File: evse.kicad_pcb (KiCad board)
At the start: 2 copper layers, 100 x 100 mm, 121 parts, among them IC1 LF353, IC2 ATmega328P, IC3 LM358, IC8 HCPL-2731S, J1 ISP, J2 Conn_01x04_Pin, J3 KF128-2.54-2P, J4 T44009, J5 T44009, J6 T44009, J7 T44009, J8 T44009, J9 T44009, K1 HF186F/12-HCTF, K2 HF186F/12-HCTF, M1 MOV, M2 MOV, M3 MOV, Q2 MMBT2222A, Q3 MMBT2222A, U1 AP63205WU, U2 TC1044S, U3 MCP9808, Y1 16MHz

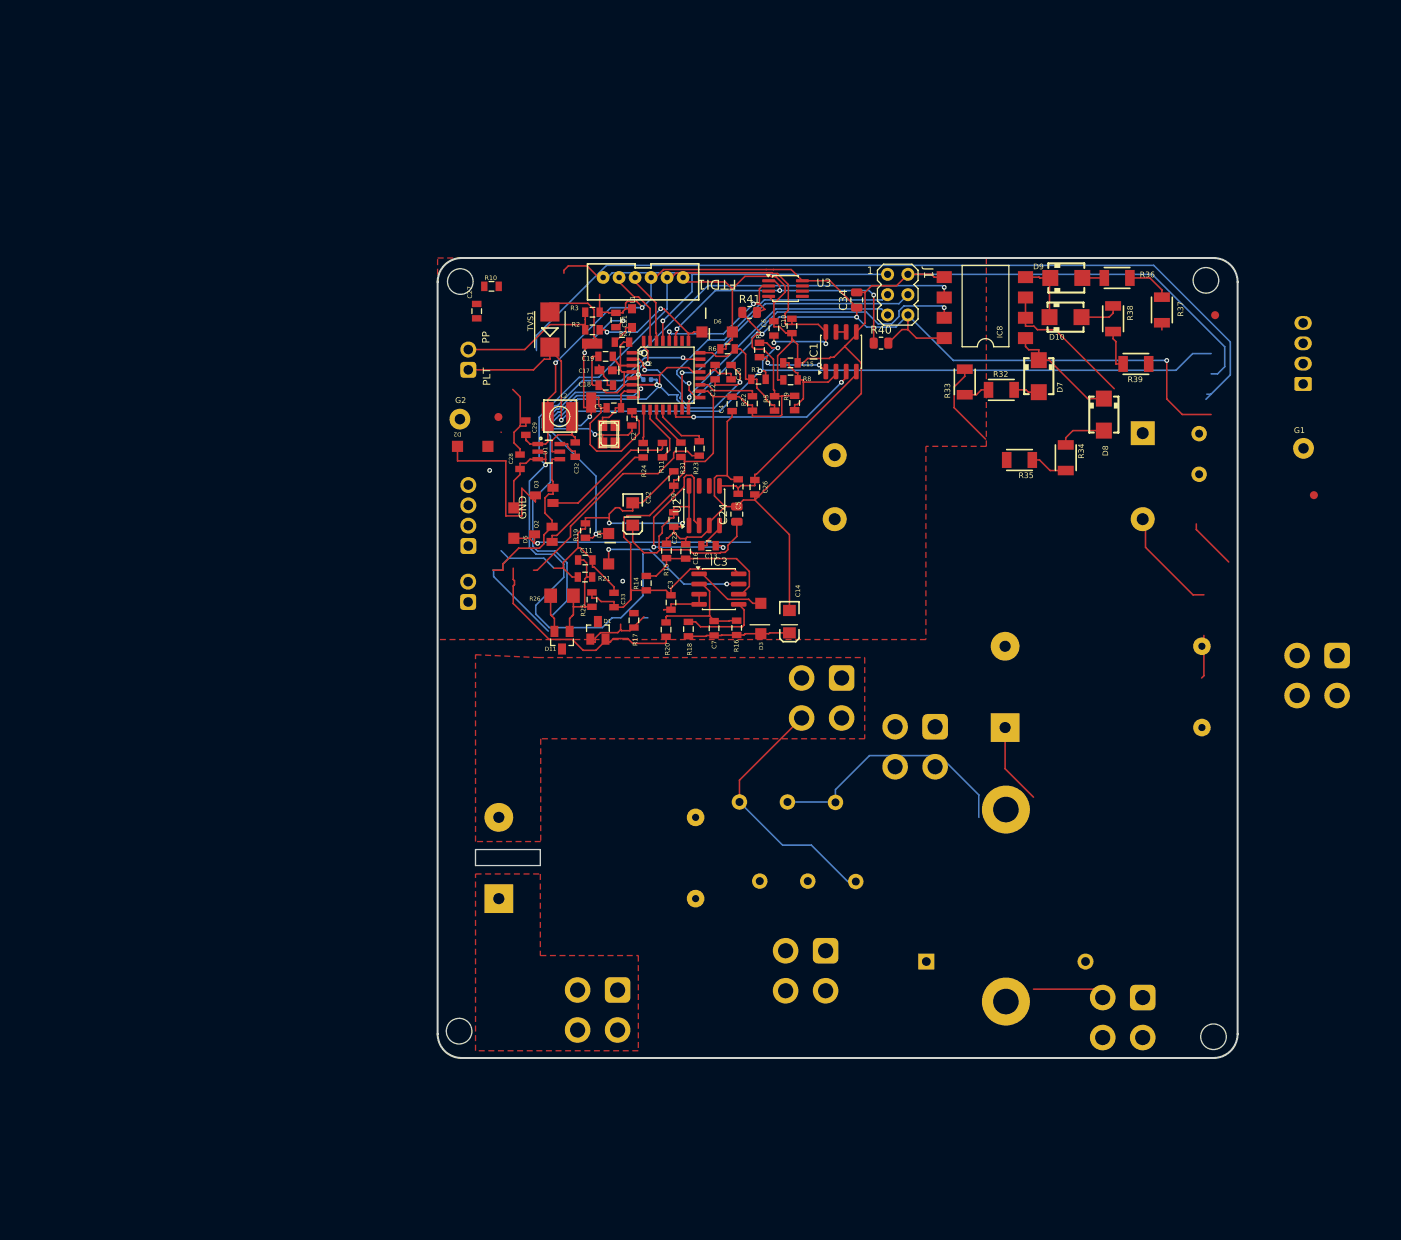
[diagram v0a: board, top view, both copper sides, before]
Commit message: Add DL-CT08CL19 GFCI transformer
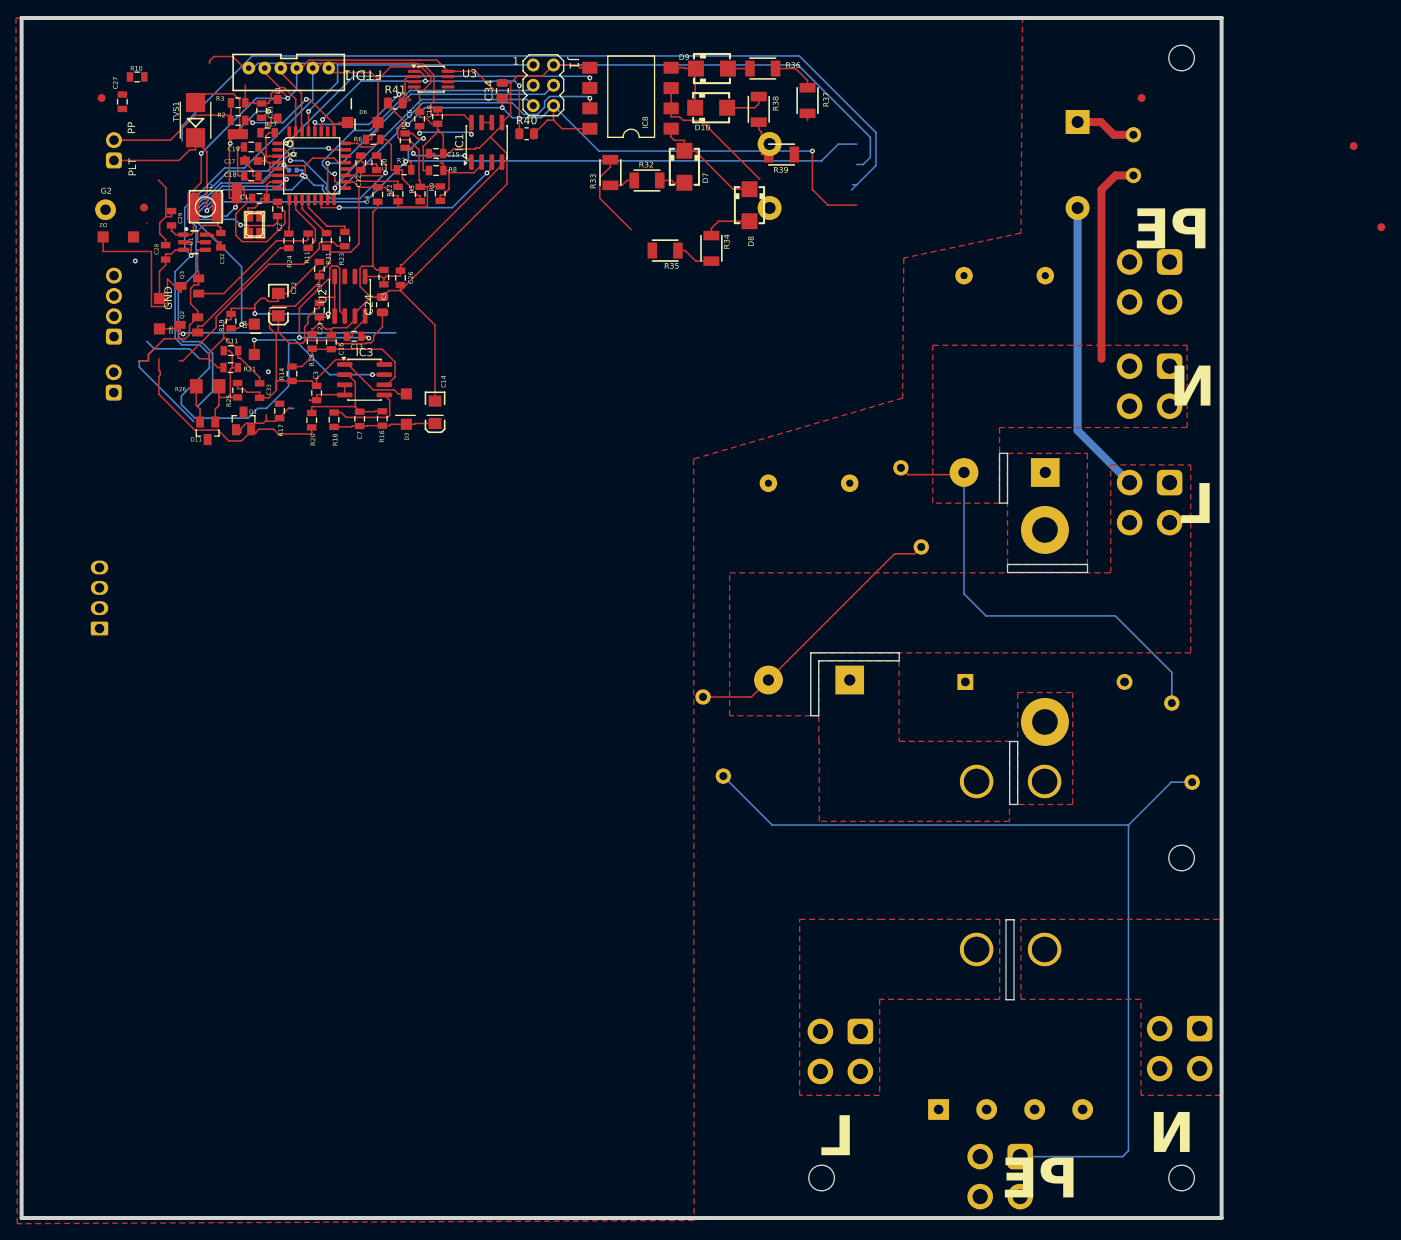
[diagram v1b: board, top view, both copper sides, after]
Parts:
- removed G1: M01PTH, 1X01
- added FID4: FIDUCIAL1X2.5, FIDUCIAL-1X2.5, F.Cu at (160.0, 30.0)
- added FID4: FIDUCIAL1X2.5, FIDUCIAL-1X2.5, F.Cu at (30.0, 30.0)
- added GFCI_CT2: DL-CT08CL19-1000/1, DL_CT:DL-CT08CL19-1000-1, B.Cu at (143.6, 136.4)
- PS1: footprint OpenEVSE:Converter_ACDC_MeanWell_IRM-10-12_THT -> Converter_ACDC:Converter_ACDC_MeanWell_IRM-10-xx_THT
- moved J2 153.5 mm to (29.7, 96.3)
- moved ? 151.5 mm to (165.0, 25.0)
- moved UNK_HOLE_1 115.4 mm to (165.0, 125.0)
- moved UNK_HOLE_0 112.2 mm to (165.0, 165.0)
- moved J8 65.1 mm to (161.0, 53.0)
- moved ? 52.1 mm to (120.0, 165.0)
- moved C10 51.5 mm to (72.0, 32.3)
- moved C18 51.5 mm to (48.7, 39.7)
- moved C23 51.5 mm to (57.2, 56.5)
- moved G2 51.5 mm to (30.5, 44.0)
- moved IC1 51.5 mm to (78.1, 35.5)
- moved PILOT1 51.5 mm to (31.5, 37.8)
- moved R16 51.5 mm to (65.1, 70.1)
- moved R34 51.5 mm to (106.2, 48.8)
- moved R35 51.5 mm to (100.4, 49.1)
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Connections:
- net Net-(D1-K2) renamed GFCI_SENSE
- net Net-(GFCI_CT1-Pin_2) renamed GFCI_TEST_DRIVE
- J4 pad 1: AC_L_OUT -> AC_L_OUT_P2
- J6 pad 1: AC_N_OUT_P2 -> AC_N_OUT_P3
- K1 pad 13: AC_L_OUT -> AC_L_OUT_P1
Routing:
- net PE: track 17.9 -> 135.8 mm
- net ACNIN: track 32.2 -> 83.3 mm
- net ACLIN: track 54.9 -> 83.0 mm
- net AC_N_OUT_P1: track 10.2 -> 0.00 mm
- net AC_N_OUT_P2: track 9.08 -> 0.00 mm
- net Net-(PS1-AC/N): track 0.00 -> 7.64 mm
- net (no net): track 6.43 -> 0.00 mm
- net +12V: track 162.6 -> 157.2 mm
- added copper zone on F.Cu, net ACNIN
- added copper zone on F.Cu, net AC_L_OUT_P1
- added copper zone on F.Cu, net AC_L_OUT_P2
- added copper zone on F.Cu, net AC_N_OUT_P1
- added copper zone on F.Cu, net AC_N_OUT_P2
- added copper zone on F.Cu, net AC_N_OUT_P3
- removed copper zone on F.Cu, net AC_L_OUT
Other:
- board size 100 x 100 mm -> 150 x 150 mm
- board text added: "L"
- board text added: "N"
- board text added: "PE"

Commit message: 18/09
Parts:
- removed CT1: DL-CT10C1.0, DL_CT:DL-CT10C1.0
- removed GFCI_CT2: DL-CT08CL19-1000/1, DL_CT:DL-CT08CL19-1000-1
- J2: value Conn_01x04_Pin -> KF128-2.54-4P; footprint Connector_Molex:Molex_KK-254_AE-6410-04A_1x04_P2.54mm_Vertical -> OpenEVSE:TerminalBlock_KF128-2.54-4P
- moved J8 141.9 mm to (29.0, 105.0)
- moved J5 132.3 mm to (29.0, 90.0)
- moved J7 132.3 mm to (29.0, 75.0)
- moved M2 124.8 mm to (43.0, 79.4), turned to 90 degrees
- moved F1 119.8 mm to (66.2, 106.1), turned to 90 degrees
- moved PS1 112.1 mm to (60.0, 97.0), turned to 90 degrees
- moved J9 107.4 mm to (50.0, 110.0)
- moved M1 93.2 mm to (38.0, 89.3)
- moved UNK_HOLE_1 86.5 mm to (79.0, 116.0)
- moved D11 70.0 mm to (112.9, 65.3)
- moved J6 67.1 mm to (110.0, 110.0)
- moved D1 66.2 mm to (112.2, 55.2)
- moved M3 65.2 mm to (43.0, 89.9)
- moved R26 62.3 mm to (105.5, 67.8)
- moved D4 59.9 mm to (109.0, 60.0)
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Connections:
- net GFCI_SENSE renamed Net-(D1-K2)
- net GFCI_TEST_DRIVE renamed Net-(GFCI_CT1-Pin_2)
- J3 pad 1: AMP_CT_SENSE -> AMP_READ
- J3 pad 2: AMP_READ -> AMP_CT_SENSE
- J4 pad 1: AC_L_OUT_P2 -> AC_L_OUT
- J6 pad 1: AC_N_OUT_P3 -> AC_N_OUT
- K1 pad 13: AC_L_OUT_P1 -> AC_L_OUT
- K2 pad 13: AC_N_OUT_P1 -> AC_N_OUT
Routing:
- net GND: track 321.1 -> 164.7 mm, vias 4 -> 1
- net PE: track 135.8 -> 17.9 mm
- net ACLIN: track 83.0 -> 10.9 mm
- net ACNIN: track 83.3 -> 31.4 mm
- net Net-(GFCI_CT1-Pin_2): track 28.3 -> 0.00 mm
- net Net-(D1-K2): track 27.7 -> 0.00 mm
- net Net-(U2-CAP+): track 27.7 -> 0.00 mm, vias 2 -> 0
- net DC_RELAY_C1: track 31.0 -> 4.57 mm
- net Net-(IC1C-V-): track 25.0 -> 0.36 mm
- net +5V: track 237.4 -> 214.7 mm
- net Net-(IC3B-OUT2): track 19.9 -> 0.00 mm, vias 2 -> 0
- net Net-(IC3B--IN2): track 18.6 -> 0.00 mm
- net +12V: track 157.2 -> 175.1 mm
- net Net-(IC3A--IN1): track 14.7 -> 0.00 mm
- net AMP_CT_SENSE: track 14.5 -> 0.00 mm
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- added copper zone on F.Cu, net AC_L_OUT
- added copper zone on F.Cu, net AC_N_OUT
- removed copper zone on F.Cu, net AC_L_OUT_P1
- removed copper zone on F.Cu, net AC_L_OUT_P2
- removed copper zone on F.Cu, net AC_N_OUT_P1
- removed copper zone on F.Cu, net AC_N_OUT_P2
- removed copper zone on F.Cu, net AC_N_OUT_P3
- removed copper zone on F.Cu, net GND
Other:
- board size 150 x 150 mm -> 123.2 x 100 mm

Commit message: test
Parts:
- moved C2 4.83 mm to (48.5, 47.2), turned to 90 degrees
- moved C1 4.74 mm to (50.7, 47.2), turned to 90 degrees
- moved Y1 2.01 mm to (49.6, 43.9), turned to 0 degrees
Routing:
- added copper zone on B.Cu, net UGND
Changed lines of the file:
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@@
 	(footprint "PCM_SparkFun-Clock:Crystal_SMD_3.2x2.5mm"
 		(layer "F.Cu")
-		(at 49.12 45.8542 90)
+		(at 49.6 43.9)
 		(property "Reference" "Y1"
 			(at 0 0 90)
@@
 		(duplicate_pad_numbers_are_jumpers no)
 		(fp_line
-			(start 1.6 -1.2)
-			(end -1.6 -1.2)
+			(start -1.6 -1.2)
+			(end -1.6 1.2)
 			(stroke
 				(width 0.127)
@@
 		)
 		(fp_line
-			(start -1.6 -1.2)
-			(end -1.6 1.2)
+			(start -1.6 1.2)
+			(end 1.6 1.2)
 			(stroke
 				(width 0.127)
@@
 		)
 		(fp_line
-			(start -1.0825 -1)
-			(end 1.0825 -1)
+			(start -1.4 0.6825)
+			(end -1.4 -0.6825)
 			(stroke
 				(width 0.127)
@@
 		)
 		(fp_line
-			(start 1.4 -0.6825)
-			(end 1.4 0.6825)
+			(start -1.0825 -1)
+			(end 1.0825 -1)
 			(stroke
 				(width 0.127)
@@
 		)
 		(fp_line
-			(start -1.4 0.6825)
-			(end -1.4 -0.6825)
+			(start 1.0825 1)
+			(end -1.0825 1)
 			(stroke
 				(width 0.127)
@@
 		)
 		(fp_line
-			(start 1.0825 1)
-			(end -1.0825 1)
+			(start 1.4 -0.6825)
+			(end 1.4 0.6825)
 			(stroke
 				(width 0.127)
@@
 		)
 		(fp_line
-			(start 1.6 1.2)
-			(end 1.6 -1.2)
+			(start 1.6 -1.2)
+			(end -1.6 -1.2)
 			(stroke
 				(width 0.127)
@@
 		)
 		(fp_line
-			(start -1.6 1.2)
-			(end 1.6 1.2)
+			(start 1.6 1.2)
+			(end 1.6 -1.2)
 			(stroke
 				(width 0.127)
@@
 		)
 		(fp_arc
-			(start 1.0825 -1)
-			(mid 1.307006 -0.907006)
-			(end 1.4 -0.6825)
+			(start -1.4 -0.6825)
+			(mid -1.307006 -0.907006)
+			(end -1.0825 -1)
 			(stroke
 				(width 0.127)
@@
 		)
 		(fp_arc
-			(start -1.4 -0.6825)
-			(mid -1.307006 -0.907006)
-			(end -1.0825 -1)
+			(start -1.0825 1)
+			(mid -1.307006 0.907006)
+			(end -1.4 0.6825)
 			(stroke
 				(width 0.127)
@@
 		)
 		(fp_arc
-			(start 1.4 0.6825)
-			(mid 1.307006 0.907006)
-			(end 1.0825 1)
+			(start 1.0825 -1)
+			(mid 1.307006 -0.907006)
+			(end 1.4 -0.6825)
 			(stroke
 				(width 0.127)
@@
 		)
 		(fp_arc
-			(start -1.0825 1)
-			(mid -1.307006 0.907006)
-			(end -1.4 0.6825)
+			(start 1.4 0.6825)
+			(mid 1.307006 0.907006)
+			(end 1.0825 1)
 			(stroke
 				(width 0.127)
@@
 	(footprint "Capacitor_SMD:C_0805_2012Metric"
 		(layer "F.Cu")
-		(at 49.728 42.5576)
+		(at 50.7 47.2 90)
 		(property "Reference" "C1"
 			(at -2.4238 0.1761 0)
@@
 	(footprint "Capacitor_SMD:C_0805_2012Metric"
 		(layer "F.Cu")
-		(at 51.9976 43.87 -90)
+		(at 48.5 47.2 90)
 		(property "Reference" "C2"
 			(at 1.7128 0.1143 90)
@@
 		(duplicate_pad_numbers_are_jumpers no)
 		(fp_line
-			(start -0.3 0.6)
-			(end 0.3 0.6)
+			(start -0.3 -0.6)
+			(end 0.3 -0.6)
 			(stroke
 				(width 0.1524)
@@
 		)
 		(fp_line
-			(start -0.3 -0.6)
-			(end 0.3 -0.6)
+			(start -0.3 0.6)
+			(end 0.3 0.6)
 			(stroke
 				(width 0.1524)
@@
 			)
 		)
+	)
+	(zone
+		(net "UGND")
+		(layer "B.Cu")
+		(hatch edge 0.5)
+		(connect_pads
+			(clearance 0.25)
+		)
+		(min_thickness 0.25)
+		(fill yes
+			(thermal_gap 0.3)
+			(thermal_bridge_width 0.3)
+			(island_removal_mode 1)
+		)
+		(polygon
+			(pts
+				(xy 45 30) (xy 67 30) (xy 67 50) (xy 45 50)
+			)
+		)

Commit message: from home
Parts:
- removed C1, C2: 12pF, Capacitor_SMD:C_0805_2012Metric
- removed C10, C13, C26, C5, C6: 10uF, Capacitor_SMD:C_0805_2012Metric
- removed C11, C32: 0.1uF, Capacitor_SMD:C_0805_2012Metric
- removed C12, C19, C21, C27: 0.1uF, PCM_SparkFun-Capacitor:C_0805_2012Metric
- removed C14: 10uf, OpenEVSE:C_1206_3216Metric_AC
- removed C15, C18, C20, C23, C24, C3, C4, C9: 1.0uF, PCM_SparkFun-Capacitor:C_0805_2012Metric
- removed C16, C7: .1uf, Capacitor_SMD:C_0805_2012Metric
- removed C17: 10uF, PCM_SparkFun-Capacitor:C_0603_1608Metric_Polar
- removed C22: 10uF, Capacitor_SMD:C_1206_3216Metric
- removed C28: 10uF, PCM_SparkFun-Capacitor:C_0805_2012Metric
- removed C29, C33: 22uF, PCM_SparkFun-Capacitor:C_0805_2012Metric
- removed C34: 100nF, Capacitor_SMD:C_0805_2012Metric
- removed C35: 0.1uF, Capacitor_SMD:C_0402_1005Metric
- removed D1: AZ23C5V6-7-F, Package_TO_SOT_SMD:SOT-23
- removed D10, D7, D8, D9: 1N4004, OpenEVSE:SMA_AC
- removed D11: AZ23C2V7, Package_TO_SOT_SMD:SOT-23
- removed D2, D5: SS14, Diode_SMD:D_SOD-123
- removed D3, D4, D6: 1N4148, OpenEVSE:SOD-123_AC
- removed FTDI1: Conn_01x06_Pin, OpenEVSE:FTDI_JST_PH_1x06_P2.00mm
- removed IC1: LF353, Package_SO:SOIC-8_3.9x4.9mm_P1.27mm
- removed IC2: ATmega328P, PCM_SparkFun-Semiconductor-Standard:TQFP-32_7x7mm_P0.8mm
- removed IC3: LM358, Package_SO:SOIC-8_3.9x4.9mm_P1.27mm
- removed IC8: HCPL-2731S, OpenEVSE:SIL8-2
- removed J1: ISP, OpenEVSE:AVR_ISP_2x03_P2.54mm
- removed L1: BLM21PG331SN1D, PCM_SparkFun-Coil:0805
- removed L2: 4.7uH, OpenEVSE:NR5040
- removed Q2, Q3: MMBT2222A, Package_TO_SOT_SMD:SOT-23
- removed R1: 620, Resistor_SMD:R_0805_2012Metric
- removed R10, R19, R2, R22, R31: 10k, Resistor_SMD:R_0805_2012Metric
- removed R11, R24: 220, Resistor_SMD:R_0805_2012Metric
- removed R14, R16, R21, R25, R6, R8, R9: 100k, Resistor_SMD:R_0805_2012Metric
- removed R15: 20k, Resistor_SMD:R_0805_2012Metric
- removed R17: 422, Resistor_SMD:R_0805_2012Metric
- removed R18: 100, Resistor_SMD:R_0805_2012Metric
- removed R20, R3: 1k, Resistor_SMD:R_0805_2012Metric
- removed R23: 330, Resistor_SMD:R_0805_2012Metric
- removed R26: 20R 1% 0.25W, Resistor_SMD:R_1206_3216Metric
- removed R27: 2, Resistor_SMD:R_0805_2012Metric
- removed R32, R33, R34, R35, R36, R37, R38, R39: 180k, Resistor_SMD:R_1210_3225Metric
- removed R40, R41: 4.7k, Resistor_SMD:R_0805_2012Metric
- removed R5: 56k, Resistor_SMD:R_0805_2012Metric
- removed R7: 200k, Resistor_SMD:R_0805_2012Metric
- removed SH1, SH2: NetTie_2, OpenEVSE:SHORT_TOP-50
- removed TVS1: P6SMB16CA, OpenEVSE:SMB
- removed U1: AP63205WU, Package_TO_SOT_SMD:TSOT-23-6
- removed U2: TC1044S, Package_SO:SOIC-8_3.9x4.9mm_P1.27mm
- removed U3: MCP9808, Package_SO:MSOP-8_3x3mm_P0.65mm
- removed Y1: 16MHz, PCM_SparkFun-Clock:Crystal_SMD_3.2x2.5mm
- moved FID4 25.8 mm to (14.6, 28.2)
- moved G2 19.1 mm to (14.7, 33.3)
- moved FID4 11.4 mm to (16.2, 23.6)
- moved J8 5.00 mm to (29.0, 110.0)
- moved J5 2.00 mm to (29.0, 92.0)
- moved M2 1.00 mm to (42.0, 79.4)
- moved M3 1.00 mm to (42.0, 89.9)
- moved M1 0.99 mm to (37.0, 89.3)
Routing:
- net +5V: track 214.7 -> 0.00 mm, vias 5 -> 0
- net GND: track 164.7 -> 1.08 mm, vias 1 -> 0
- net PP: track 123.3 -> 0.00 mm
- net PILOT: track 114.3 -> 0.00 mm, vias 3 -> 0
- net +12V: track 175.1 -> 80.7 mm, vias 3 -> 0
- net UGND: track 76.6 -> 0.00 mm, vias 6 -> 0
- net RESET: track 52.2 -> 0.00 mm, vias 1 -> 0
- net GMI_LINE: track 50.8 -> 0.00 mm, vias 2 -> 0
- net WELD_DETECT: track 43.9 -> 0.00 mm, vias 2 -> 0
- net AMP_READ: track 43.3 -> 0.00 mm, vias 1 -> 0
- net MOSI: track 36.9 -> 0.00 mm, vias 1 -> 0
- net SDA: track 36.6 -> 0.00 mm, vias 3 -> 0
- net AVR_SCK: track 35.4 -> 0.00 mm, vias 1 -> 0
- net MISO: track 31.4 -> 0.00 mm, vias 1 -> 0
- net Net-(IC2-XTAL2/PB7): track 28.6 -> 0.00 mm, vias 2 -> 0
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- added copper zone on F.Cu, net PE
- removed copper zone on B.Cu, net UGND
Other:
- board size 123.2 x 100 mm -> 100 x 100 mm
- board text removed: "AC"
- board text removed: "GND"
- board text removed: "PLT"
- board text removed: "PP"
